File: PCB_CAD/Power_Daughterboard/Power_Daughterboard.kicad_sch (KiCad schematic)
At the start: 5 parts, among them J1 470531000, J2 CMF2.1111.12

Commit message: power daughterboard work
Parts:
- added PSU_bulk1: 100u, Capacitor_SMD:C_0805_2012Metric_Pad1.18x1.45mm_HandSolder, symbol Device:C_Polarized_Small_US
- added PSU_noise1: 0.1u, Capacitor_SMD:C_0805_2012Metric_Pad1.18x1.45mm_HandSolder, symbol Device:C_Small
- F1: footprint FUSE_SS-5H-1A_EAT -> CustomModels:FUSE_SS-5H-1A_EAT
- J1: footprint CONN_SD-47053-001_H10p00_MOL -> CustomModels:CONN_SD-47053-001_H10p00_MOL
- J2: footprint CONN4_1131.12_SAI -> CustomModels:CONN4_1131.12_SAI
- PS1: footprint HP02S0300WI -> CustomModels:HP02S0300WI
- RV1: footprint MOV14D561KTR -> CustomModels:MOV14D561KTR
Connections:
- net at J1.1, PS1.3 (DC-): now also PSU_bulk1.2, PSU_noise1.1
- net at J1.2, PS1.4 (DC+): now also PSU_bulk1.1, PSU_noise1.2
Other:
- moved on the sheet: J1

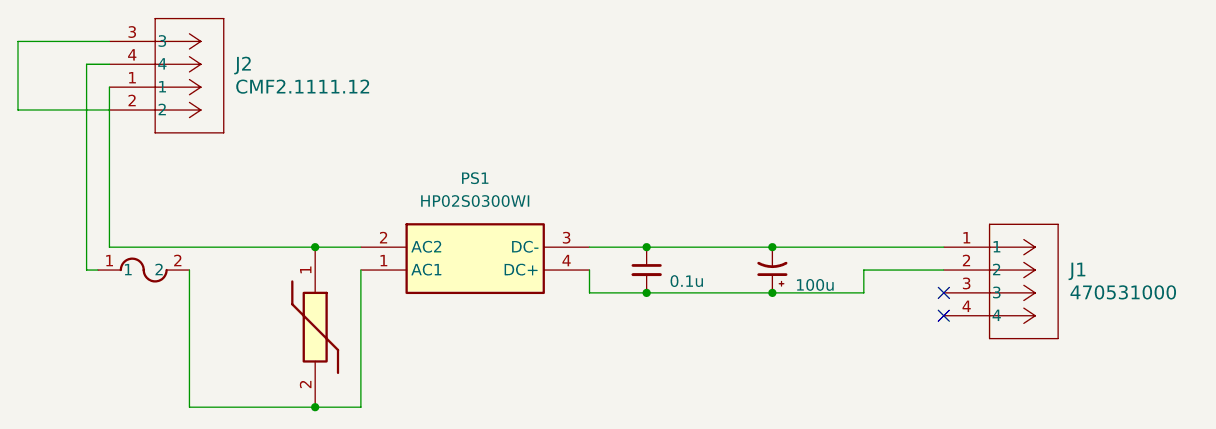
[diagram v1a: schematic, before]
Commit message: work on power daughterboard
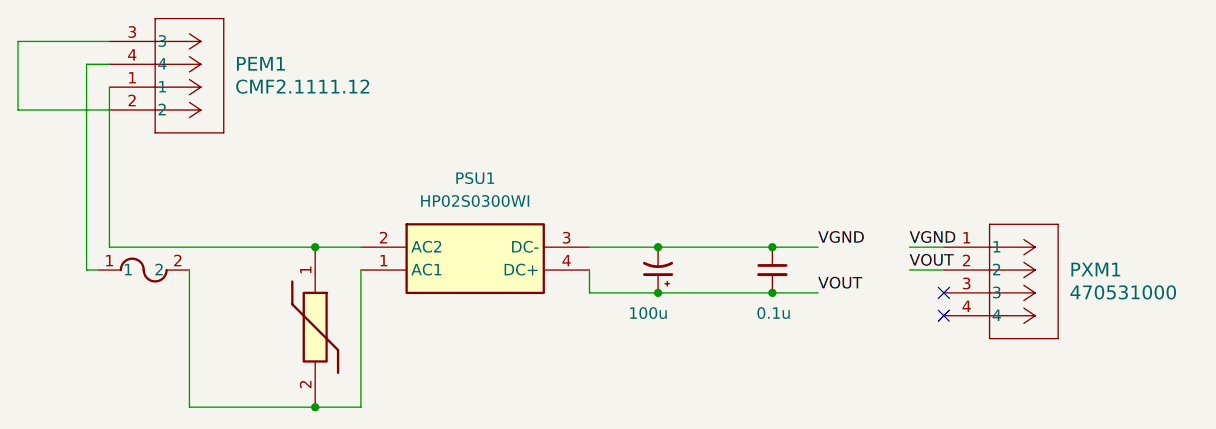
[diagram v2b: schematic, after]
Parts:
- renumbered PSU_bulk1 to Cb1, PSU_noise1 to Cn1, F1 to FUSE1, RV1 to MOV1, J2 to PEM1, PS1 to PSU1, J1 to PXM1
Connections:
- net VGND: now reaches Cb1.2, Cn1.1, PSU1.3 (DC-), PXM1.1
- net VOUT: now reaches Cb1.1, Cn1.2, PSU1.4 (DC+), PXM1.2
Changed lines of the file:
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@@
 	(paper "A4")
+	(junction
+		(at 93.98 57.15)
+		(diameter 0)
+		(color 0 0 0 0)
+	)
+	(junction
+		(at 93.98 52.07)
+		(diameter 0)
+		(color 0 0 0 0)
+	)
+	(junction
+		(at 106.68 52.07)
+		(diameter 0)
+		(color 0 0 0 0)
+	)
+	(junction
+		(at 55.88 69.85)
+		(diameter 0)
+		(color 0 0 0 0)
+	)
+	(junction
+		(at 55.88 52.07)
+		(diameter 0)
+		(color 0 0 0 0)
+	)
 	(junction
 		(at 106.68 57.15)
@@
 		(color 0 0 0 0)
 	)
-	(junction
-		(at 92.71 52.07)
-		(diameter 0)
-		(color 0 0 0 0)
-	)
-	(junction
-		(at 106.68 52.07)
-		(diameter 0)
-		(color 0 0 0 0)
-	)
-	(junction
-		(at 92.71 57.15)
-		(diameter 0)
-		(color 0 0 0 0)
-	)
-	(junction
-		(at 55.88 69.85)
-		(diameter 0)
-		(color 0 0 0 0)
-	)
-	(junction
-		(at 55.88 52.07)
-		(diameter 0)
-		(color 0 0 0 0)
-	)
 	(no_connect
 		(at 125.73 57.15)
@@
 	(wire
 		(pts
-			(xy 92.71 57.15) (xy 106.68 57.15)
-		)
-		(stroke
-			(width 0)
-			(type default)
-		)
-	)
-	(wire
-		(pts
-			(xy 106.68 57.15) (xy 116.84 57.15)
+			(xy 121.92 54.61) (xy 125.73 54.61)
 		)
 		(stroke
@@
 	(wire
 		(pts
-			(xy 116.84 57.15) (xy 116.84 54.61)
+			(xy 121.92 52.07) (xy 125.73 52.07)
 		)
 		(stroke
@@
 	(wire
 		(pts
-			(xy 116.84 54.61) (xy 125.73 54.61)
-		)
-		(stroke
-			(width 0)
-			(type default)
-		)
-	)
-	(wire
-		(pts
-			(xy 86.36 52.07) (xy 92.71 52.07)
-		)
-		(stroke
-			(width 0)
-			(type default)
-		)
-	)
-	(wire
-		(pts
-			(xy 86.36 57.15) (xy 92.71 57.15)
+			(xy 86.36 52.07) (xy 93.98 52.07)
+		)
+		(stroke
+			(width 0)
+			(type default)
+		)
+	)
+	(wire
+		(pts
+			(xy 106.68 52.07) (xy 111.76 52.07)
+		)
+		(stroke
+			(width 0)
+			(type default)
+		)
+	)
+	(wire
+		(pts
+			(xy 86.36 57.15) (xy 93.98 57.15)
 		)
 		(stroke
@@
 	(wire
 		(pts
+			(xy 106.68 57.15) (xy 111.76 57.15)
+		)
+		(stroke
+			(width 0)
+			(type default)
+		)
+	)
+	(wire
+		(pts
 			(xy 30.48 31.75) (xy 30.48 54.61)
 		)
@@
 	(wire
 		(pts
-			(xy 106.68 52.07) (xy 125.73 52.07)
+			(xy 93.98 57.15) (xy 106.68 57.15)
+		)
+		(stroke
+			(width 0)
+			(type default)
+		)
+	)
+	(wire
+		(pts
+			(xy 93.98 52.07) (xy 106.68 52.07)
 		)
 		(stroke
@@
 	(wire
 		(pts
-			(xy 92.71 52.07) (xy 106.68 52.07)
-		)
-		(stroke
-			(width 0)
-			(type default)
-		)
-	)
-	(wire
-		(pts
 			(xy 22.86 36.83) (xy 22.86 29.21)
 		)
@@
 			(width 0)
 			(type default)
+		)
+	)
+	(label "VOUT"
+		(at 111.76 57.15 0)
+		(fields_autoplaced yes)
+		(effects
+			(font
+				(size 1.27 1.27)
+			)
+			(justify left bottom)
+		)
+	)
+	(label "VOUT"
+		(at 121.92 54.61 0)
+		(fields_autoplaced yes)
+		(effects
+			(font
+				(size 1.27 1.27)
+			)
+			(justify left bottom)
+		)
+	)
+	(label "VGND"
+		(at 111.76 52.07 0)
+		(fields_autoplaced yes)
+		(effects
+			(font
+				(size 1.27 1.27)
+			)
+			(justify left bottom)
+		)
+	)
+	(label "VGND"
+		(at 121.92 52.07 0)
+		(fields_autoplaced yes)
+		(effects
+			(font
+				(size 1.27 1.27)
+			)
+			(justify left bottom)
 		)
 	)
@@
 		(dnp no)
 		(fields_autoplaced yes)
-		(property "Reference" "RV1"
+		(property "Reference" "MOV1"
 			(at 59.69 59.6899 90)
 			(effects
@@
 			(project ""
 				(path "/90df3e27-f695-4db1-b86b-e403ac5fc296"
-					(reference "RV1")
+					(reference "MOV1")
 					(unit 1)
 				)
@@
 		(dnp no)
 		(fields_autoplaced yes)
-		(property "Reference" "PS1"
+		(property "Reference" "PSU1"
 			(at 73.66 44.45 0)
 			(effects
@@
 			(project ""
 				(path "/90df3e27-f695-4db1-b86b-e403ac5fc296"
-					(reference "PS1")
+					(reference "PSU1")
 					(unit 1)
 				)
@@
 	(symbol
 		(lib_id "Device:C_Polarized_Small_US")
-		(at 106.68 54.61 180)
+		(at 93.98 54.61 180)
 		(unit 1)
 		(exclude_from_sim no)
@@
 		(on_board yes)
 		(dnp no)
-		(fields_autoplaced yes)
-		(property "Reference" "PSU_bulk1"
-			(at 109.22 53.7717 0)
+		(property "Reference" "Cb1"
+			(at 96.52 53.7717 0)
 			(effects
 				(font
@@
 		)
 		(property "Value" "100u"
-			(at 109.22 56.3117 0)
+			(at 90.678 59.436 0)
 			(effects
 				(font
@@
 		)
 		(property "Footprint" "Capacitor_SMD:C_0805_2012Metric_Pad1.18x1.45mm_HandSolder"
-			(at 106.68 54.61 0)
+			(at 93.98 54.61 0)
 			(effects
 				(font
@@
 		)
 		(property "Datasheet" "~"
-			(at 106.68 54.61 0)
+			(at 93.98 54.61 0)
 			(effects
 				(font
@@
 		)
 		(property "Description" "electrolytic"
-			(at 106.68 54.61 0)
+			(at 93.98 54.61 0)
 			(effects
 				(font
@@
 			(project ""
 				(path "/90df3e27-f695-4db1-b86b-e403ac5fc296"
-					(reference "PSU_bulk1")
+					(reference "Cb1")
 					(unit 1)
 				)
@@
 		(dnp no)
 		(fields_autoplaced yes)
-		(property "Reference" "J1"
+		(property "Reference" "PXM1"
 			(at 139.7 54.6099 0)
 			(effects
@@
 			(project ""
 				(path "/90df3e27-f695-4db1-b86b-e403ac5fc296"
-					(reference "J1")
+					(reference "PXM1")
 					(unit 1)
 				)
@@
 		(dnp no)
 		(fields_autoplaced yes)
-		(property "Reference" "F1"
+		(property "Reference" "FUSE1"
 			(at 36.83 48.26 0)
 			(effects
@@
 			(project ""
 				(path "/90df3e27-f695-4db1-b86b-e403ac5fc296"
-					(reference "F1")
+					(reference "FUSE1")
 					(unit 1)
 				)
@@
 	(symbol
 		(lib_id "Device:C_Small")
-		(at 92.71 54.61 0)
+		(at 106.68 54.61 0)
 		(unit 1)
 		(exclude_from_sim no)
@@
 		(on_board yes)
 		(dnp no)
-		(fields_autoplaced yes)
-		(property "Reference" "PSU_noise1"
-			(at 95.25 53.3462 0)
+		(property "Reference" "Cn1"
+			(at 109.22 53.3462 0)
 			(effects
 				(font
@@
 		)
 		(property "Value" "0.1u"
-			(at 95.25 55.8862 0)
+			(at 104.902 59.436 0)
 			(effects
 				(font
@@
 		)
 		(property "Footprint" "Capacitor_SMD:C_0805_2012Metric_Pad1.18x1.45mm_HandSolder"
-			(at 92.71 54.61 0)
+			(at 106.68 54.61 0)
 			(effects
 				(font
@@
 		)
 		(property "Datasheet" "~"
-			(at 92.71 54.61 0)
+			(at 106.68 54.61 0)
 			(effects
 				(font
@@
 		)
 		(property "Description" "ceramic, acap (to PSU)"
-			(at 92.71 54.61 0)
+			(at 106.68 54.61 0)
 			(effects
 				(font
@@
 			(project ""
 				(path "/90df3e27-f695-4db1-b86b-e403ac5fc296"
-					(reference "PSU_noise1")
+					(reference "Cn1")
 					(unit 1)
 				)
@@
 		(dnp no)
 		(fields_autoplaced yes)
-		(property "Reference" "J2"
+		(property "Reference" "PEM1"
 			(at 46.99 31.7499 0)
 			(effects
@@
 			(project ""
 				(path "/90df3e27-f695-4db1-b86b-e403ac5fc296"
-					(reference "J2")
+					(reference "PEM1")
 					(unit 1)
 				)

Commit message: power daughterboard finished
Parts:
- C1: renamed from Cb1; value 100u -> 0.1u; footprint Capacitor_SMD:C_0805_2012Metric_Pad1.18x1.45mm_HandSolder -> Capacitor_THT:C_Rect_L4.6mm_W2.0mm_P2.50mm_MKS02_FKP02; symbol Device:C_Polarized_Small_US -> Device:C_Small
- C2: renamed from Cn1; value 0.1u -> 1u; footprint Capacitor_SMD:C_0805_2012Metric_Pad1.18x1.45mm_HandSolder -> Capacitor_THT:C_Rect_L4.6mm_W2.0mm_P2.50mm_MKS02_FKP02
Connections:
- net VGND: no longer names the net of C1.2, PSU1.3 (DC-), PXM1.1
- net VGND: now also C2.2; no longer C2.1
- net VOUT: no longer names the net of C1.1, PSU1.4 (DC+), PXM1.2
- net VOUT: now also C2.1; no longer C2.2
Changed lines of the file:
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@@
-	(wire
-		(pts
-			(xy 121.92 52.07) (xy 125.73 52.07)
-		)
-		(stroke
-			(width 0)
-			(type default)
-		)
-	)
 	(wire
 		(pts
@@
 	(wire
 		(pts
-			(xy 106.68 52.07) (xy 111.76 52.07)
+			(xy 121.92 57.15) (xy 121.92 54.61)
+		)
+		(stroke
+			(width 0)
+			(type default)
+		)
+	)
+	(wire
+		(pts
+			(xy 106.68 52.07) (xy 125.73 52.07)
 		)
 		(stroke
@@
 	(wire
 		(pts
-			(xy 106.68 57.15) (xy 111.76 57.15)
+			(xy 106.68 57.15) (xy 121.92 57.15)
 		)
 		(stroke
@@
 			(width 0)
 			(type default)
-		)
-	)
-	(label "VOUT"
-		(at 111.76 57.15 0)
-		(fields_autoplaced yes)
-		(effects
-			(font
-				(size 1.27 1.27)
-			)
-			(justify left bottom)
-		)
-	)
-	(label "VOUT"
-		(at 121.92 54.61 0)
-		(fields_autoplaced yes)
-		(effects
-			(font
-				(size 1.27 1.27)
-			)
-			(justify left bottom)
-		)
-	)
-	(label "VGND"
-		(at 111.76 52.07 0)
-		(fields_autoplaced yes)
-		(effects
-			(font
-				(size 1.27 1.27)
-			)
-			(justify left bottom)
-		)
-	)
-	(label "VGND"
-		(at 121.92 52.07 0)
-		(fields_autoplaced yes)
-		(effects
-			(font
-				(size 1.27 1.27)
-			)
-			(justify left bottom)
 		)
 	)
@@
 	)
 	(symbol
-		(lib_id "Device:C_Polarized_Small_US")
+		(lib_id "Device:C_Small")
 		(at 93.98 54.61 180)
 		(unit 1)
@@
 		(on_board yes)
 		(dnp no)
-		(property "Reference" "Cb1"
+		(property "Reference" "C1"
 			(at 96.52 53.7717 0)
 			(effects
@@
 			)
 		)
-		(property "Value" "100u"
+		(property "Value" "0.1u"
 			(at 90.678 59.436 0)
 			(effects
@@
 			)
 		)
-		(property "Footprint" "Capacitor_SMD:C_0805_2012Metric_Pad1.18x1.45mm_HandSolder"
+		(property "Footprint" "Capacitor_THT:C_Rect_L4.6mm_W2.0mm_P2.50mm_MKS02_FKP02"
 			(at 93.98 54.61 0)
 			(effects
@@
 			)
 		)
-		(property "Description" "electrolytic"
+		(property "Description" "ceramic, closer to PSU"
 			(at 93.98 54.61 0)
 			(effects
@@
 			(project ""
 				(path "/90df3e27-f695-4db1-b86b-e403ac5fc296"
-					(reference "Cb1")
+					(reference "C1")
 					(unit 1)
 				)
@@
 		(lib_id "Device:C_Small")
 		(at 106.68 54.61 0)
+		(mirror x)
 		(unit 1)
 		(exclude_from_sim no)
@@
 		(on_board yes)
 		(dnp no)
-		(property "Reference" "Cn1"
-			(at 109.22 53.3462 0)
+		(property "Reference" "C2"
+			(at 109.22 55.8738 0)
 			(effects
 				(font
@@
 			)
 		)
-		(property "Value" "0.1u"
-			(at 104.902 59.436 0)
+		(property "Value" "1u"
+			(at 104.902 49.784 0)
 			(effects
 				(font
@@
 			)
 		)
-		(property "Footprint" "Capacitor_SMD:C_0805_2012Metric_Pad1.18x1.45mm_HandSolder"
+		(property "Footprint" "Capacitor_THT:C_Rect_L4.6mm_W2.0mm_P2.50mm_MKS02_FKP02"
 			(at 106.68 54.61 0)
 			(effects
@@
 			)
 		)
-		(property "Description" "ceramic, acap (to PSU)"
+		(property "Description" "ceramic, closer to PXM"
 			(at 106.68 54.61 0)
 			(effects
@@
 			(project ""
 				(path "/90df3e27-f695-4db1-b86b-e403ac5fc296"
-					(reference "Cn1")
+					(reference "C2")
 					(unit 1)
 				)
